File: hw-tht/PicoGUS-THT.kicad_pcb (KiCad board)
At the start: 2 copper layers, 103.7 x 99.8 mm, 82 parts, among them J1 IRQDMA_JP, J3 Bus_ISA_8bit, J5 SJ1-3535NG, J6 UART_TX, J7 USB power jumper, J8 SJ1-3535NG-GR, J9 Waveblaster, U1 Pico, U10 74AHCT126, U11 NE5532, U2 74AHC244, U3 SN74CB3T3257, U4 SN74CB3T3257, U5 74AHC14, U6 74AHC00, U7 74AHC00, U8 APS6404L-3SQR-SN, U9 PCM5100A

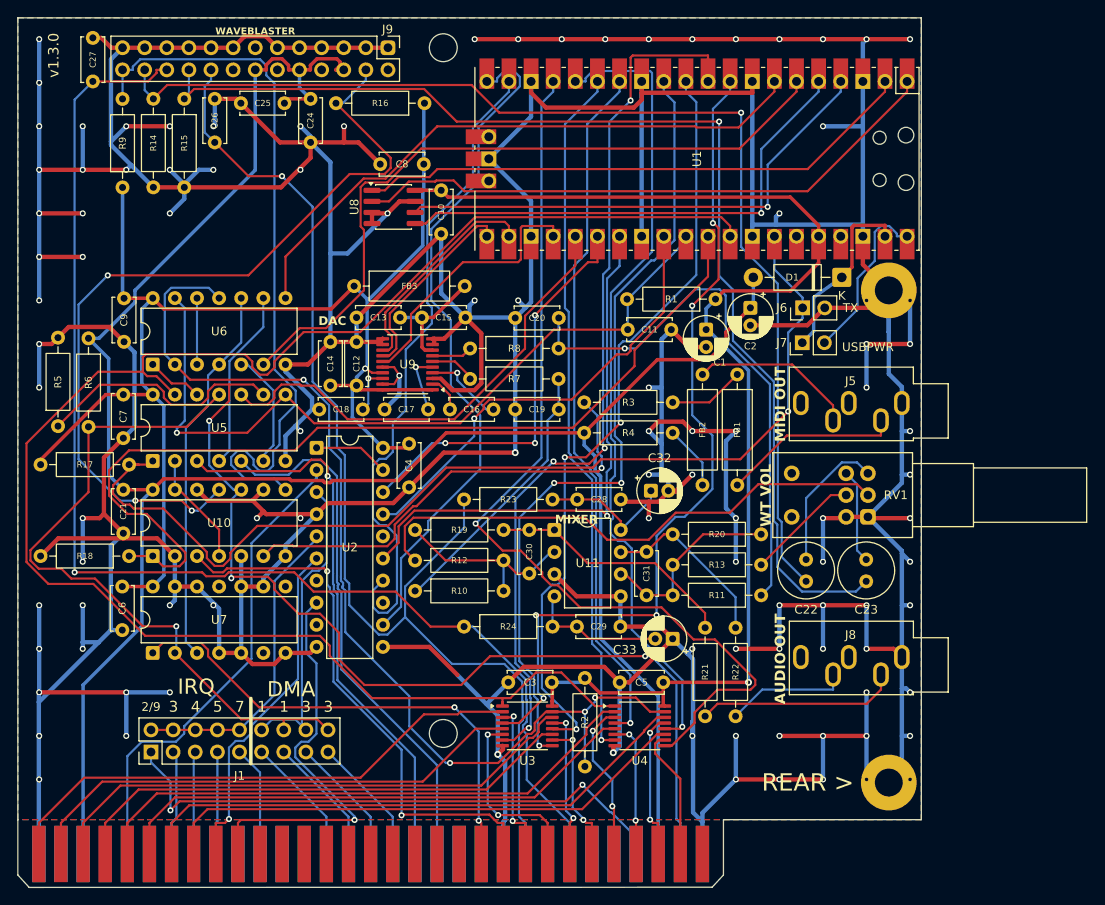
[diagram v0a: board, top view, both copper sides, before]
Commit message: hw-tht: GY-PCM5102 module option (J10) as an either/or alternative to the DAC
- J10 (new footprint PiGUS library:GY-PCM5102_Module + symbol): the module plugs
  in on female headers - its I2S row (SCK->GND, BCK, DIN, LCK, GND, VIN=+5V) and
  the AGND/ROUT/AGND/LROUT end of its 9-pin row, as I2S_DAC1/J4 on v1.2. Its
  outputs join U9's (DAC_OUTL/R) ahead of R7/R8 + C19/C20, so the mixer, WT path
  and firmware are unchanged. Fit U9 + C12-C18 + FB3 OR the module, never both.
- Placed right of the Waveblaster area over low parts (courtyard only around the
  pins); R4 and C28 moved a few mm. Oval pads keep two tracks per gap.
- Silkscreen: dashed "DAC" outline around the parts to leave out for the module
  (R7/R8 notched out: they stay), heading "DAC -OR- J10 MODULE", dashed module
  outline labelled "J10: GY-PCM5102".
- BOM: J10 module + 1x6/1x4 female headers as optional lines; U9 note.
- README: DAC option section with the fit/leave-out table.
- Re-routed around the module: 0 DRC errors, 0 unconnected, schematic parity OK;
  ERC 0 errors.

Co-Authored-By: Claude Opus 5.5 <noreply@anthropic.com>
Claude-Session: https://claude.ai/code/session_011utN3x8yYUNDvkpGCEq5yD
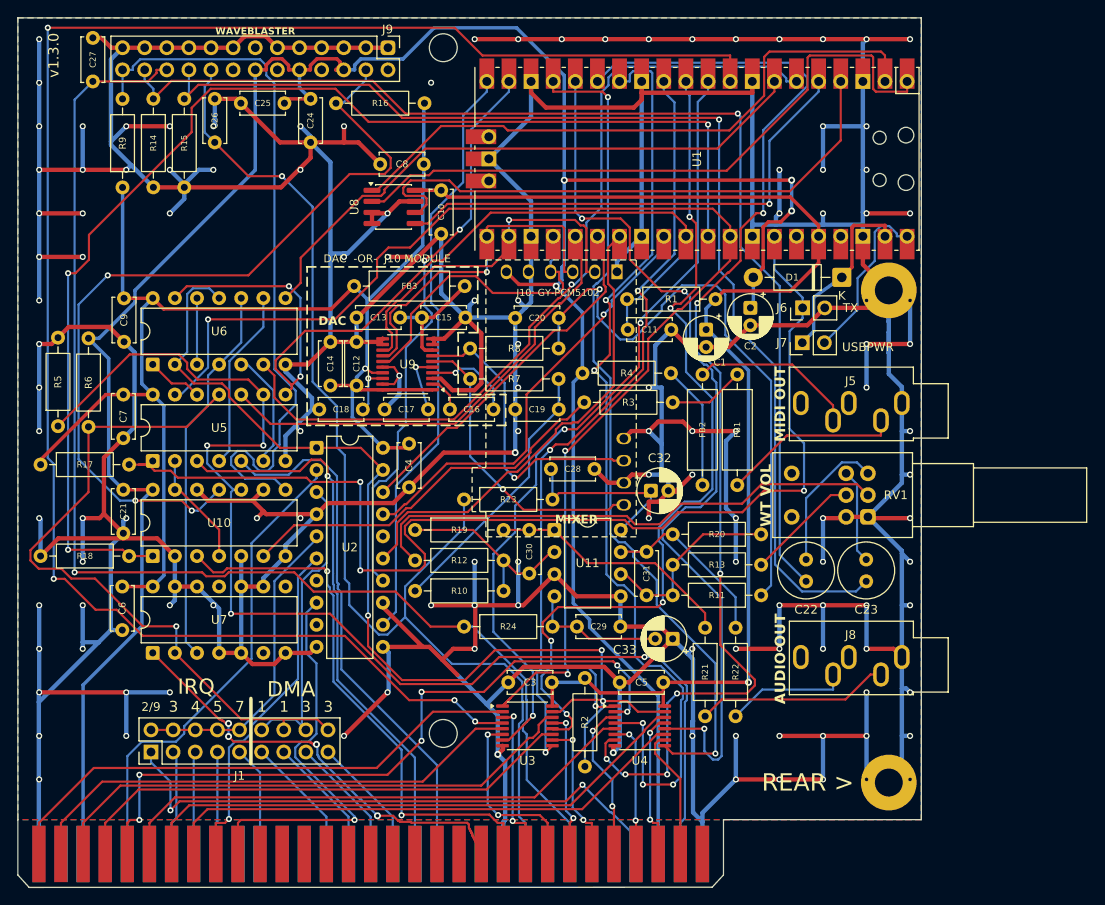
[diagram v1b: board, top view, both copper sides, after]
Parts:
- added J10: GY-PCM5102, PiGUS library:GY-PCM5102_Module, F.Cu at (178.0, 80.3)
- moved R4 6.85 mm to (191.4, 77.0)
- moved C28 4.62 mm to (177.6, 88.0)
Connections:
- net Net-(U9-OUTL) renamed /PCM5100 audio/DAC_OUTL
- net Net-(U9-OUTR) renamed /PCM5100 audio/DAC_OUTR
- J3 pad 11: (no net) -> unconnected-(J3-~{SMEMW}-Pad11)
- J3 pad 12: (no net) -> unconnected-(J3-~{SMEMR}-Pad12)
- J3 pad 19: (no net) -> unconnected-(J3-~{DACK0}-Pad19)
- J3 pad 20: (no net) -> unconnected-(J3-CLK-Pad20)
- J3 pad 22: (no net) -> unconnected-(J3-IRQ6-Pad22)
- J3 pad 26: (no net) -> unconnected-(J3-~{DACK2}-Pad26)
- J3 pad 28: (no net) -> unconnected-(J3-ALE-Pad28)
- J3 pad 30: (no net) -> unconnected-(J3-OSC-Pad30)
- J3 pad 32: (no net) -> unconnected-(J3-IO-Pad32)
- J3 pad 43: (no net) -> unconnected-(J3-BA19-Pad43)
- J3 pad 44: (no net) -> unconnected-(J3-BA18-Pad44)
- J3 pad 45: (no net) -> unconnected-(J3-BA17-Pad45)
- J3 pad 46: (no net) -> unconnected-(J3-BA16-Pad46)
- J3 pad 47: (no net) -> unconnected-(J3-BA15-Pad47)
- J3 pad 48: (no net) -> unconnected-(J3-BA14-Pad48)
- J3 pad 49: (no net) -> unconnected-(J3-BA13-Pad49)
- J3 pad 5: (no net) -> unconnected-(J3--5V-Pad5)
- J3 pad 50: (no net) -> unconnected-(J3-BA12-Pad50)
- J3 pad 51: (no net) -> unconnected-(J3-BA11-Pad51)
- J3 pad 52: (no net) -> unconnected-(J3-BA10-Pad52)
- J3 pad 6: (no net) -> unconnected-(J3-DRQ2-Pad6)
- J3 pad 8: (no net) -> unconnected-(J3-UNUSED-Pad8)
- J5 pad RN: (no net) -> unconnected-(J5-PadRN)
- J5 pad TN: (no net) -> unconnected-(J5-PadTN)
- J9 pad 12: (no net) -> unconnected-(J9-Pin_12-Pad12)
- J9 pad 13: (no net) -> unconnected-(J9-Pin_13-Pad13)
- J9 pad 16: (no net) -> unconnected-(J9-Pin_16-Pad16)
- J9 pad 2: (no net) -> unconnected-(J9-Pin_2-Pad2)
- J9 pad 8: (no net) -> unconnected-(J9-Pin_8-Pad8)
- U1 pad 35: (no net) -> unconnected-(U1-ADC_VREF-Pad35)
- U1 pad 37: (no net) -> unconnected-(U1-3V3_EN-Pad37)
- U1 pad 41: (no net) -> unconnected-(U1-SWCLK-Pad41)
- U1 pad 43: (no net) -> unconnected-(U1-SWDIO-Pad43)
- U2 pad 16: (no net) -> unconnected-(U2-1Y1-Pad16)
- U2 pad 7: (no net) -> unconnected-(U2-2Y2-Pad7)
- U2 pad 9: (no net) -> unconnected-(U2-2Y3-Pad9)
- U7 pad 11: (no net) -> unconnected-(U7-Pad11)
- U7 pad 6: (no net) -> unconnected-(U7-Pad6)
- U7 pad 8: (no net) -> unconnected-(U7-Pad8)
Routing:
- net GND: track 1165.2 -> 1274.3 mm, vias 102 -> 126
- net AD0: track 97.5 -> 204.6 mm, vias 5 -> 4
- net AD5: track 80.4 -> 134.1 mm, vias 1 -> 7
- net +5V: track 262.3 -> 303.9 mm, vias 0 -> 4
- net ADS: track 194.2 -> 157.6 mm, vias 0 -> 4
- net ~{RI/OCHRDY}: track 106.2 -> 141.9 mm, vias 0 -> 3
- net /PCM5100 audio/DAC_OUTR: track 4.67 -> 35.1 mm, vias 0 -> 1
- net AD4: track 80.3 -> 109.7 mm, vias 1 -> 5
- net /PCM5100 audio/DAC_OUTL: track 5.30 -> 34.5 mm, vias 0 -> 1
- net DIN: track 22.7 -> 39.5 mm, vias 0 -> 1
- net A4: track 65.3 -> 81.5 mm, vias 0 -> 6
- net BCK: track 25.4 -> 41.2 mm, vias 0 -> 1
- net UART_TX: track 119.0 -> 132.5 mm, vias 1 -> 3
- net ~{RIOW}: track 82.9 -> 95.9 mm, vias 0 -> 1
- net AD7: track 108.9 -> 96.9 mm, vias 1 -> 2
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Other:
- board text added: "DAC -OR- J10 MODULE"
- board text added: "J10: GY-PCM5102"

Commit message: hw-tht: R7/R8 + C19/C20 belong to the DAC area; module feeds AUDIO_L/R
The GY-PCM5102 module already has the PCM510x reference 470R/2.2nF output
filter, so J10's ROUT/LROUT now join AUDIO_L/R after R7/R8 + C19/C20 instead of
U9's outputs. The whole filter is left out with the DAC when the module is used
(no double filter, no extra 470R in front of the mixer).

- Dashed DAC outline now encloses U9, C12-C20, FB3, R7, R8 (steps under J10's
  pin row); "J10: GY-PCM5102" label moved inside the module outline.
- Schematic note, BOM notes and README table updated.
- Re-routed the four audio nets: 0 DRC errors, 0 unconnected, parity OK; ERC 0.

Co-Authored-By: Claude Opus 5.5 <noreply@anthropic.com>
Claude-Session: https://claude.ai/code/session_011utN3x8yYUNDvkpGCEq5yD
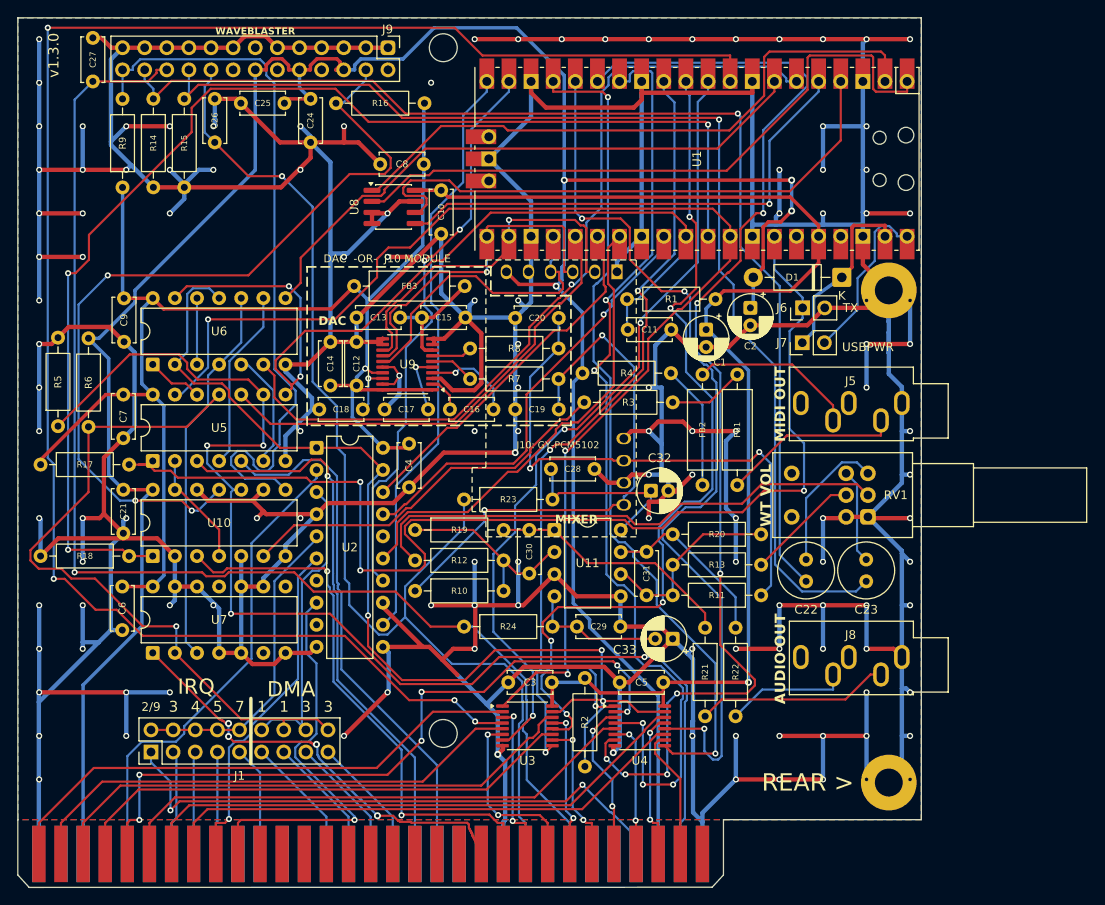
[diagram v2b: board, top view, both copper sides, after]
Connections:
- J10 pad 13: /PCM5100 audio/DAC_OUTR -> /PCM5100 audio/AUDIO_R
- J10 pad 15: /PCM5100 audio/DAC_OUTL -> /PCM5100 audio/AUDIO_L
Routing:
- net /PCM5100 audio/DAC_OUTR: track 35.1 -> 4.67 mm, vias 1 -> 0
- net /PCM5100 audio/AUDIO_L: track 31.2 -> 61.0 mm, vias 0 -> 2
- net /PCM5100 audio/DAC_OUTL: track 34.5 -> 5.15 mm, vias 1 -> 0
- net /PCM5100 audio/AUDIO_R: track 69.1 -> 63.4 mm, vias 1 -> 2
- net ADS: track 157.6 -> 160.7 mm
- net +3V3: track 303.5 -> 304.9 mm
- net GND: track 1274.3 -> 1274.9 mm, vias 126 -> 127
- net AD3: track 87.8 -> 87.2 mm

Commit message: hw-tht: adopt the new DAC/GY-PCM5102 placement; re-routed; artwork moved
- Placement from the updated board: the DAC block (U9, C12-C20, FB3, R7, R8)
  moved 3 mm right and J10 now lies almost flat over it, so the module's dashed
  outline covers exactly the parts to leave out; heading "DAC -OR- GY-PCM5102".
  R3/R4 turned vertical next to C1/FB2. C32 label moved off R3's pad.
- Tracks at the moved parts ripped up and re-routed (autorouter + grid router
  for the stragglers), dangling stubs removed, U9 pin 16 stitched to GND.
  0 DRC errors, 0 unconnected, schematic parity OK.
- Back artwork regenerated at its new spot above the ISA fingers (pad cut-outs
  recomputed there), dedication where it was placed.
- The module is soldered almost flat on its male pins: the 8.5 mm female header
  lines are gone from the BOM (sockets would hit a Waveblaster board). README.

Co-Authored-By: Claude Opus 5.5 <noreply@anthropic.com>
Claude-Session: https://claude.ai/code/session_011utN3x8yYUNDvkpGCEq5yD
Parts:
- moved J10 13.0 mm to (166.2, 75.0), turned to 0 degrees
- moved R4 10.2 mm to (187.0, 86.2), turned to 90 degrees
- moved R3 10.1 mm to (190.5, 76.0), turned to -90 degrees
- moved C12 3.00 mm to (158.3, 73.4)
- moved C13 3.00 mm to (158.3, 70.6)
- moved C14 3.00 mm to (155.3, 73.4)
- moved C15 3.00 mm to (165.8, 70.6)
- moved C16 3.00 mm to (169.0, 81.2)
- moved C17 3.00 mm to (166.5, 81.2)
- moved C18 3.00 mm to (159.0, 81.2)
- moved C19 3.00 mm to (176.5, 81.2)
- moved C20 3.00 mm to (176.5, 70.7)
- moved R7 3.00 mm to (171.3, 77.7)
- moved R8 3.00 mm to (171.3, 74.2)
- moved U9 3.00 mm to (164.1, 76.0)
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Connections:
- J10 pad 13: /PCM5100 audio/AUDIO_R -> /PCM5100 audio/DAC_OUTR
- J10 pad 15: /PCM5100 audio/AUDIO_L -> /PCM5100 audio/DAC_OUTL
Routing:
- net +5V: track 303.9 -> 335.3 mm, vias 4 -> 5
- net RDRQ: track 50.6 -> 82.1 mm, vias 1 -> 7
- net /PCM5100 audio/AUDIO_L: track 61.0 -> 32.6 mm, vias 2 -> 0
- net /PCM5100 audio/AUDIO_R: track 63.4 -> 43.1 mm, vias 2 -> 3
- net GND: track 1274.9 -> 1290.5 mm, vias 127 -> 131
- net /PCM5100 audio/DAC_OUTL: track 5.15 -> 18.6 mm
- net +3V3: track 304.9 -> 317.7 mm
- net Net-(R3-Pad1): track 44.4 -> 55.0 mm
- net RTC: track 41.8 -> 52.2 mm
- net AD1: track 90.6 -> 100.8 mm, vias 3 -> 7
- net LRCK: track 34.8 -> 45.0 mm, vias 0 -> 1
- net DIN: track 39.5 -> 30.3 mm
- net Net-(FB1-Pad1): track 8.75 -> 17.0 mm
- net BCK: track 41.2 -> 33.3 mm
- net /PCM5100 audio/DAC_OUTR: track 4.67 -> 12.5 mm
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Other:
- board text added: "DAC -OR- GY-PCM5102"
- board text removed: "DAC -OR- J10 MODULE"
- board text removed: "J10: GY-PCM5102"
